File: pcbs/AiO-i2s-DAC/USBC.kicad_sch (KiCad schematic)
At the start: 7 parts, among them J5 USB4105-GF-A

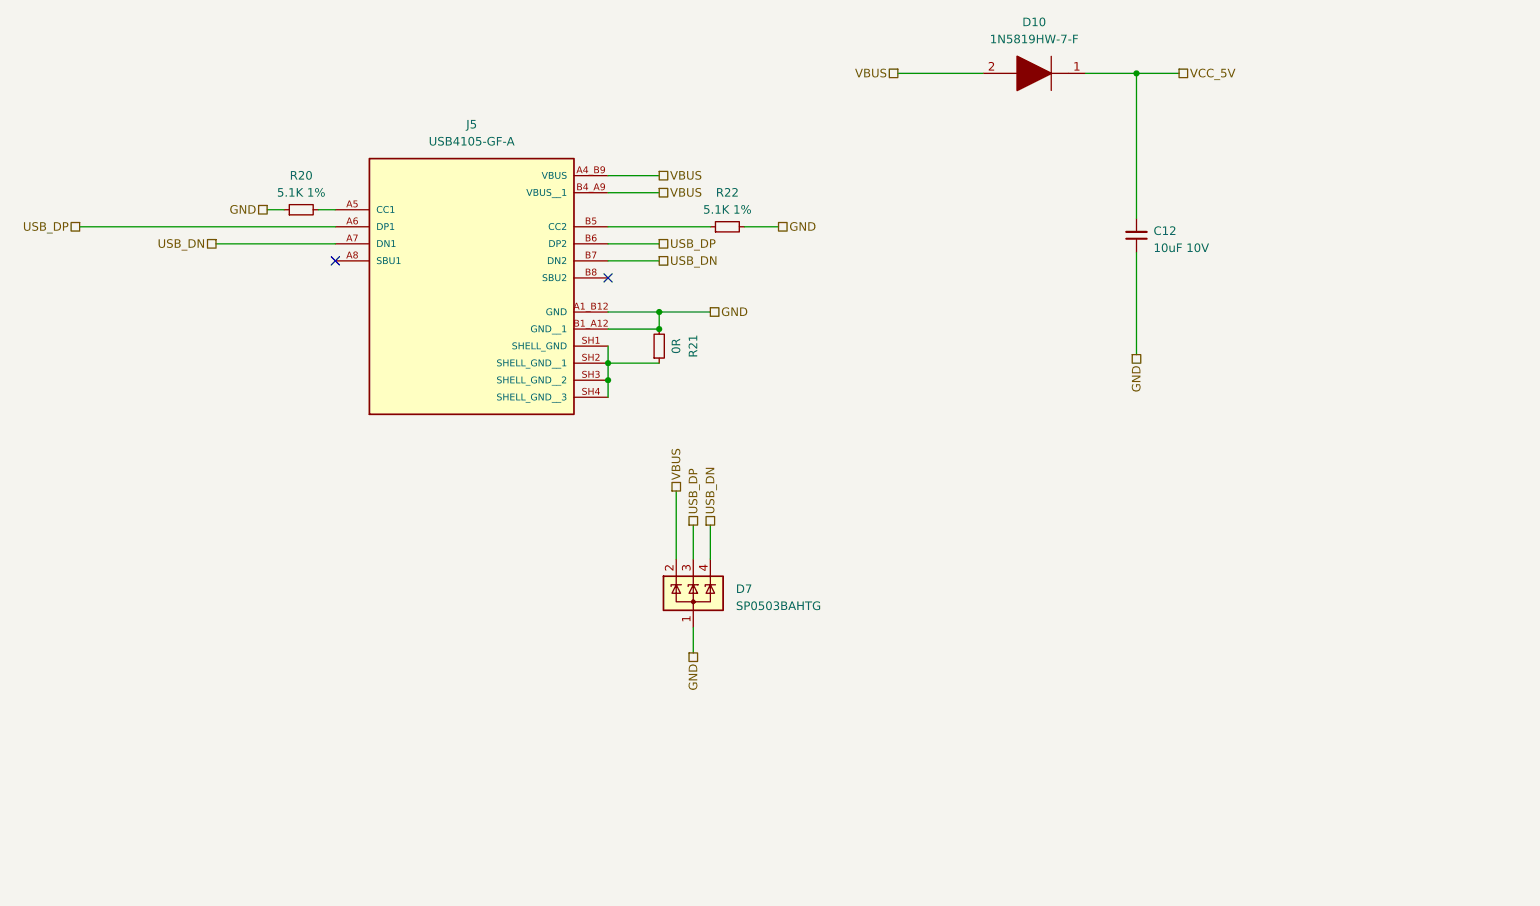
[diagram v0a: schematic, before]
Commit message: Adding equivalent JLCPCB values
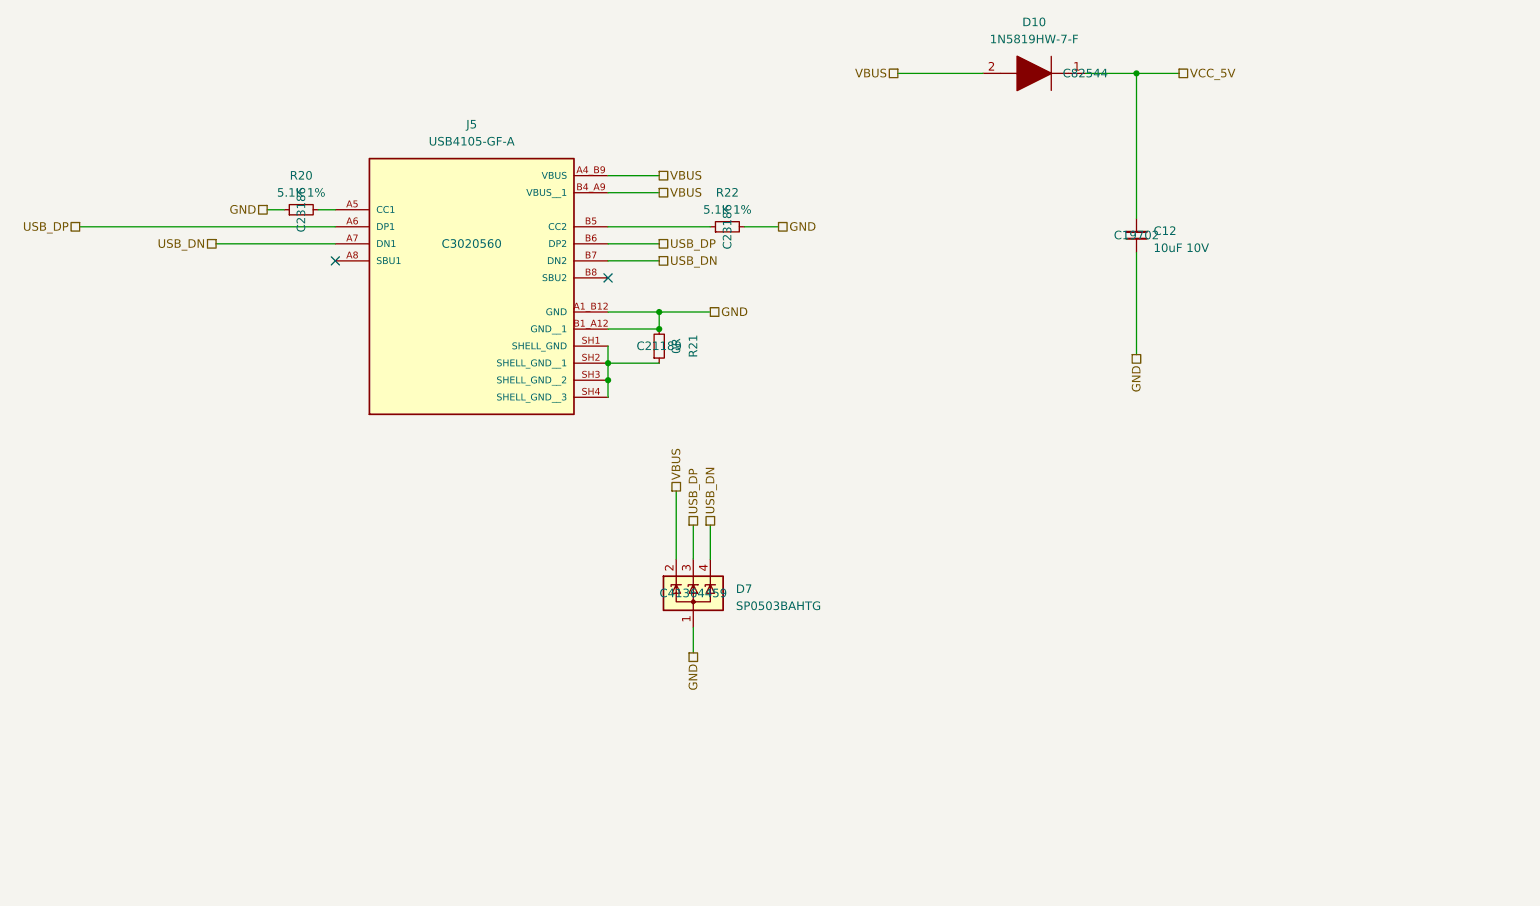
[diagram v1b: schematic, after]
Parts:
- C12: LCSC (none) -> C19702
- D10: Arrow Part Number 1N5819HW-7-F -> (none); Arrow Price/Stock https://www.arrow.com/en/products/1n5819hw-7-f/diodes-incor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 -> (none); LCSC (none) -> C82544; Mouser Part Number 621-1N5819HW-F -> (none); Mouser Price/Stock https://www.mouser.co.uk/ProductDetail/Diodes-Incorporated/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 -> (none)
- D7: LCSC (none) -> C41364459
- J5: LCSC (none) -> C3020560
- R20, R22: LCSC (none) -> C23186
- R21: LCSC (none) -> C21189
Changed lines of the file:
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@@
+			)
+		)
+		(property "LCSC" "C3020560"
+			(at 85.09 58.42 0)
+			(effects
+				(font
+					(size 1.27 1.27)
+				)
 			)
 		)
@@
 			)
 		)
+		(property "LCSC" "C23186"
+			(at 123.19 55.88 0)
+			(effects
+				(font
+					(size 1.27 1.27)
+				)
+			)
+		)
 		(pin "1"
 		)
@@
 			)
 		)
+		(property "LCSC" "C21189"
+			(at 113.03 73.66 0)
+			(effects
+				(font
+					(size 1.27 1.27)
+				)
+			)
+		)
 		(pin "1"
 		)
@@
 			)
 		)
-		(property "Mouser Part Number" "621-1N5819HW-F"
-			(at 165.1 17.78 0)
-			(effects
-				(font
-					(size 1.27 1.27)
-				)
-				(justify left)
-				(hide yes)
-			)
-		)
-		(property "Mouser Price/Stock" "https://www.mouser.co.uk/ProductDetail/Diodes-Incorporated/1N5819HW-7-F?qs=NQ47qNm99eDyWTEd07miYA%3D%3D"
-			(at 165.1 15.24 0)
-			(effects
-				(font
-					(size 1.27 1.27)
-				)
-				(justify left)
-				(hide yes)
-			)
-		)
-		(property "Arrow Part Number" "1N5819HW-7-F"
-			(at 165.1 12.7 0)
-			(effects
-				(font
-					(size 1.27 1.27)
-				)
-				(justify left)
-				(hide yes)
-			)
-		)
-		(property "Arrow Price/Stock" "https://www.arrow.com/en/products/1n5819hw-7-f/diodes-incorporated?utm_currency=USD&region=nac"
-			(at 165.1 10.16 0)
-			(effects
-				(font
-					(size 1.27 1.27)
-				)
-				(justify left)
-				(hide yes)
-			)
-		)
 		(property "Instructions/Notes" ""
 			(at 176.53 33.02 0)
@@
 				)
 				(hide yes)
+			)
+		)
+		(property "LCSC" "C82544"
+			(at 176.53 33.02 0)
+			(effects
+				(font
+					(size 1.27 1.27)
+				)
 			)
 		)
@@
 			)
 		)
+		(property "LCSC" "C23186"
+			(at 59.69 53.34 0)
+			(effects
+				(font
+					(size 1.27 1.27)
+				)
+			)
+		)
 		(pin "1"
 		)
@@
 			)
 		)
+		(property "LCSC" "C19702"
+			(at 184.15 57.15 0)
+			(effects
+				(font
+					(size 1.27 1.27)
+				)
+			)
+		)
 		(pin "1"
 		)
@@
 			)
 		)
+		(property "LCSC" "C41364459"
+			(at 118.11 110.49 0)
+			(effects
+				(font
+					(size 1.27 1.27)
+				)
+			)
+		)

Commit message: LCSC BOM Preparation
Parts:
- C12: LCSC alt (none) -> C6119842
- D10: LCSC alt (none) -> C82544
- D7: LCSC alt (none) -> C7074
- J5: LCSC alt (none) -> C3020560
- R20, R22: LCSC alt (none) -> C23186
- R21: LCSC alt (none) -> C21189
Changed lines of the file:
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@@
+			)
+		)
+		(property "LCSC alt" "C3020560"
+			(at 85.09 58.42 0)
+			(effects
+				(font
+					(size 1.27 1.27)
+				)
 			)
 		)
@@
 			)
 		)
+		(property "LCSC alt" "C23186"
+			(at 123.19 55.88 0)
+			(effects
+				(font
+					(size 1.27 1.27)
+				)
+			)
+		)
 		(pin "1"
 		)
@@
 			)
 		)
+		(property "LCSC alt" "C21189"
+			(at 113.03 73.66 0)
+			(effects
+				(font
+					(size 1.27 1.27)
+				)
+			)
+		)
 		(pin "1"
 		)
@@
 			)
 		)
+		(property "LCSC alt" "C82544"
+			(at 176.53 33.02 0)
+			(effects
+				(font
+					(size 1.27 1.27)
+				)
+			)
+		)
 		(pin "1"
 		)
@@
 			)
 		)
+		(property "LCSC alt" "C23186"
+			(at 59.69 53.34 0)
+			(effects
+				(font
+					(size 1.27 1.27)
+				)
+			)
+		)
 		(pin "1"
 		)
@@
 			)
 		)
+		(property "LCSC alt" "C6119842"
+			(at 184.15 57.15 0)
+			(effects
+				(font
+					(size 1.27 1.27)
+				)
+			)
+		)
 		(pin "1"
 		)
@@
 			(at 118.11 110.49 0)
 			(effects
+				(font
+					(size 1.27 1.27)
+				)
+			)
+		)
+		(property "LCSC alt" "C7074"
+			(at 118.11 110.49 0)
+			(effects

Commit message: Build prep
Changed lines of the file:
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@@
 					(size 1.27 1.27)
 				)
+				(hide yes)
 			)
 		)
@@
 					(size 1.27 1.27)
 				)
+				(hide yes)
 			)
 		)
@@
 					(size 1.27 1.27)
 				)
+				(hide yes)
 			)
 		)
@@
 					(size 1.27 1.27)
 				)
+				(hide yes)
 			)
 		)
@@
 					(size 1.27 1.27)
 				)
+				(hide yes)
 			)
 		)
@@
 					(size 1.27 1.27)
 				)
+				(hide yes)
 			)
 		)
@@
 					(size 1.27 1.27)
 				)
+				(hide yes)
 			)
 		)
@@
 					(size 1.27 1.27)
 				)
+				(hide yes)
 			)
 		)
@@
 					(size 1.27 1.27)
 				)
+				(hide yes)
 			)
 		)
@@
 					(size 1.27 1.27)
 				)
+				(hide yes)
 			)
 		)
@@
 					(size 1.27 1.27)
 				)
+				(hide yes)
 			)
 		)
@@
 					(size 1.27 1.27)
 				)
+				(hide yes)
 			)
 		)
@@
 					(size 1.27 1.27)
 				)
+				(hide yes)
 			)
 		)
@@
 					(size 1.27 1.27)
 				)
-			)
-		)
+				(hide yes)
+			)
+		)

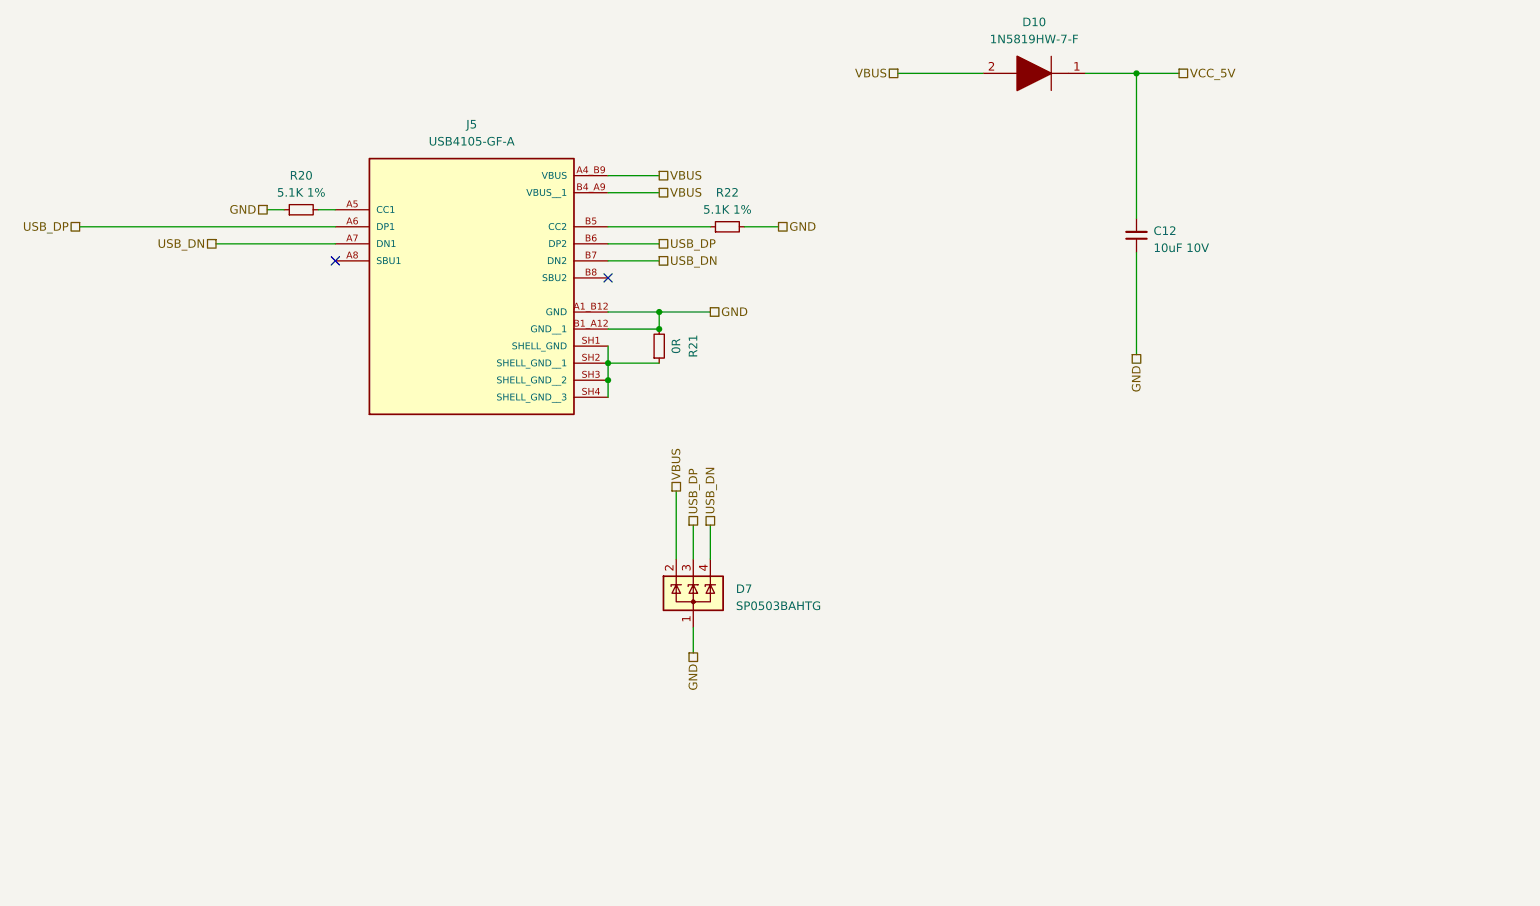
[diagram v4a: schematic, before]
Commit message: Preliminary S3 version schematic and layout
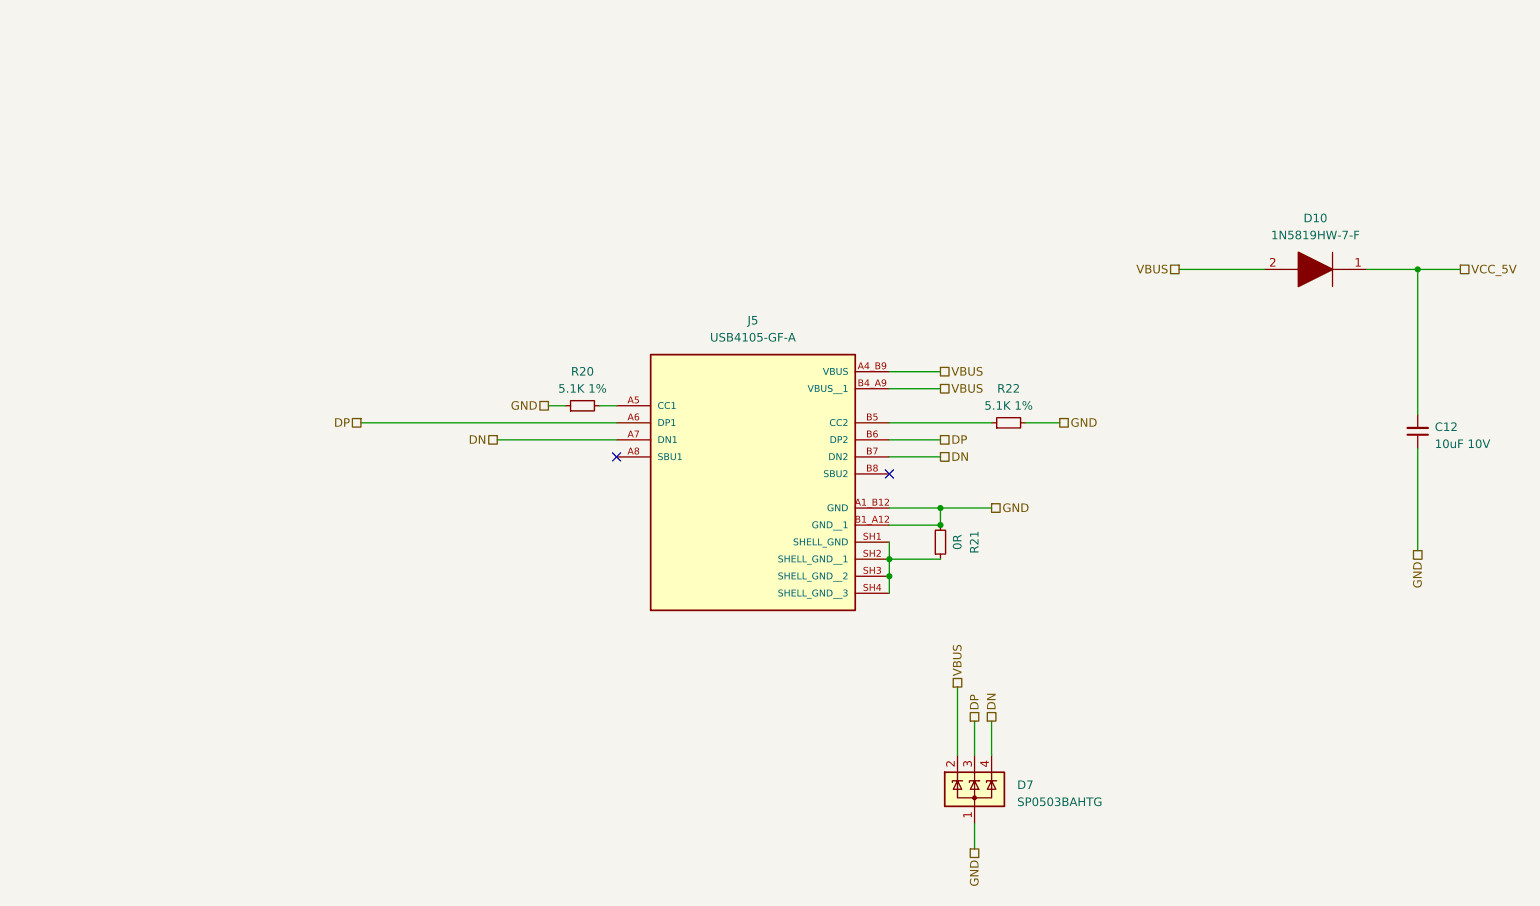
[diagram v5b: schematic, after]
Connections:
- net USB_DN renamed DN
- net USB_DP renamed DP
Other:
- moved on the sheet: C12, D10, D7, J5, R20, R21, R22
